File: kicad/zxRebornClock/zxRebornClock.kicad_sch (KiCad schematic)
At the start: 87 parts, among them J1 Conn_01x04, J2 Conn_01x03, J3 USB_B_Micro, Q1 MMBTA42, Q11 MMBTA42, Q2 MMBTA42, Q3 MMBTA42, Q4 MMBTA42, Q5 MMBTA42, Q6 MMBTA42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

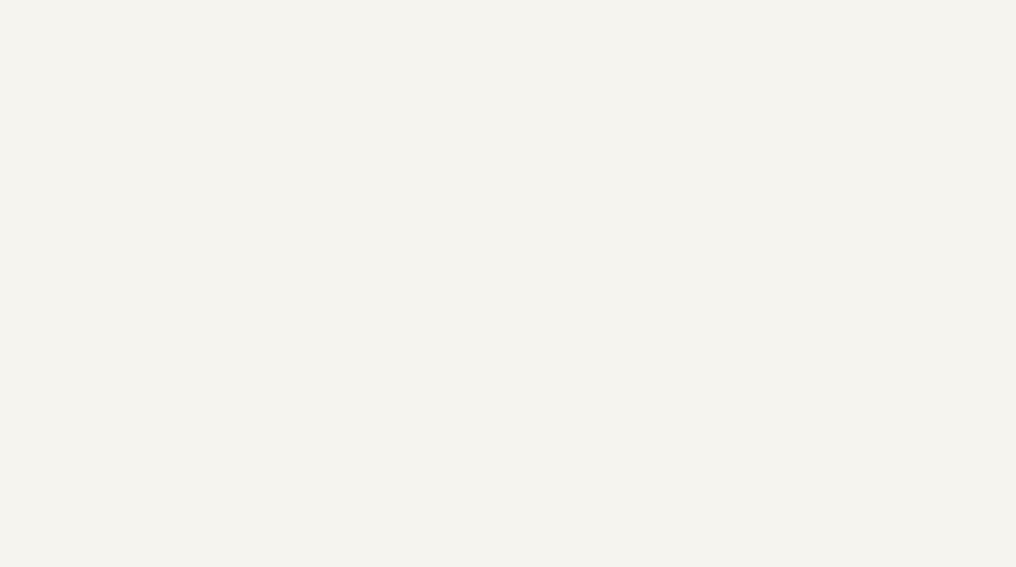
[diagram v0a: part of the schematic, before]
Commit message: add power 3.3V
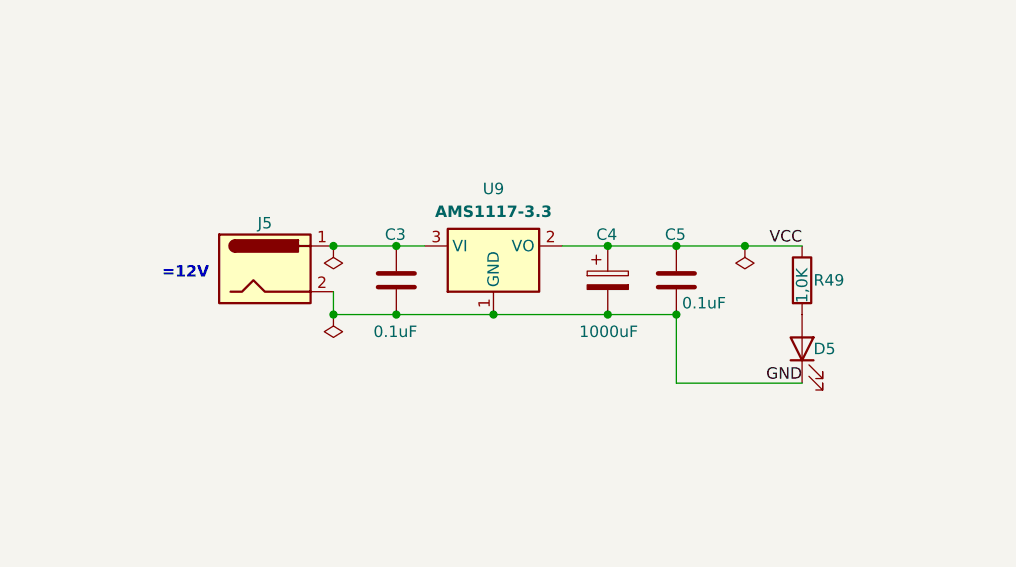
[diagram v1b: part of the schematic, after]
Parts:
- added C3, C5: 0.1uF, Capacitor_SMD:C_0805_2012Metric_Pad1.18x1.45mm_HandSolder, symbol Device:C
- added C4: 1000uF, Capacitor_THT:CP_Radial_D8.0mm_P3.50mm, symbol Device:C_Polarized
- added D5: LED, LED_SMD:LED_0805_2012Metric_Pad1.15x1.40mm_HandSolder, symbol Device:LED
- added J5: Jack DC, Connector_BarrelJack:BarrelJack_Horizontal, symbol Connector:Jack-DC
- added R49: 1,0K, Resistor_SMD:R_0805_2012Metric_Pad1.20x1.40mm_HandSolder, symbol Device:R
- added U9: AMS1117-3.3, Package_TO_SOT_SMD:SOT-223-3_TabPin2, symbol Regulator_Linear:AMS1117-5.0
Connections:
- net GND: now also C3.2, C4.2, C5.2, D5.1 (K), J5.2, U9.1 (GND)
- net VCC: now also C4.1, C5.1, R49.1, U9.2 (VO)
- new net: D5.2 (A), R49.2
- new net: C3.1, J5.1, U9.3 (VI)
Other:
- note added: "=12V"

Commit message: add some fixes
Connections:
- net VBUS: now also C3.1, J5.1, U9.3 (VI)
- net at Q7.1 (B), R26.2: now also R27.2
- net at Q1.1 (B), R2.2: now also R3.2
- net at Q8.1 (B), R28.2: now also R29.2
- net at R7.2: now also Q3.1 (B), R6.2
- net at R23.2: now also Q5.1 (B), R10.2
- net at Q2.1 (B), R4.2: now also R5.2
- net at R11.2: now also Q11.1 (B), R1.2
- net at R25.2: now also Q6.1 (B), R24.2
- net at R31.2: now also Q9.1 (B), R30.2
- net at Q4.1 (B), R8.2: now also R9.2
- no-connect marks 23 -> 37
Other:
- moved on the sheet: J5, R11, R23, R25, R27, R29, R3, R31, R5, R7, R9

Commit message: fix GPIO0 on esp12f
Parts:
- added R50: 10K, symbol Device:R
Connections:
- net VCC: now also R50.1
- net at U7.18 (GPIO0): now also R50.2
- no-connect marks 37 -> 36
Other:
- moved on the sheet: R39
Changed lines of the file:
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@@
 	)
 	(no_connect
-		(at 355.6 158.75)
-	)
-	(no_connect
 		(at 101.6 86.36)
 	)
@@
 	(wire
 		(pts
+			(xy 355.6 158.75) (xy 371.475 158.75)
+		)
+		(stroke
+			(width 0)
+			(type default)
+		)
+	)
+	(wire
+		(pts
 			(xy 355.6 36.83) (xy 355.6 27.94)
 		)
@@
 	(wire
 		(pts
+			(xy 355.6 163.83) (xy 371.475 163.83)
+		)
+		(stroke
+			(width 0)
+			(type default)
+		)
+	)
+	(wire
+		(pts
 			(xy 86.36 50.8) (xy 93.98 50.8)
 		)
@@
 		)
 	)
+	(label "VCC"
+		(at 379.095 158.75 0)
+		(effects
+			(font
+				(size 1.27 1.27)
+			)
+			(justify left bottom)
+		)
+	)
 	(label "GND"
 		(at 386.08 128.27 180)
@@
 	)
 	(label "VCC"
-		(at 363.22 163.83 0)
+		(at 379.095 163.83 0)
 		(effects
 			(font
@@
 	(symbol
 		(lib_id "Device:R")
+		(at 375.285 158.75 270)
+		(unit 1)
+		(exclude_from_sim no)
+		(in_bom yes)
+		(on_board yes)
+		(dnp no)
+		(property "Reference" "R50"
+			(at 375.031 156.718 90)
+			(effects
+				(font
+					(size 1.27 1.27)
+				)
+			)
+		)
+		(property "Value" "10K"
+			(at 375.285 158.75 90)
+			(effects
+				(font
+					(size 1.27 1.27)
+				)
+			)
+		)
+		(property "Footprint" ""
+			(at 375.285 156.972 90)
+			(effects
+				(font
+					(size 1.27 1.27)
+				)
+				(hide yes)
+			)
+		)
+		(property "Datasheet" "~"
+			(at 375.285 158.75 0)
+			(effects
+				(font
+					(size 1.27 1.27)
+				)
+				(hide yes)
+			)
+		)
+		(property "Description" "Resistor"
+			(at 375.285 158.75 0)
+			(effects
+				(font
+					(size 1.27 1.27)
+				)
+				(hide yes)
+			)
+		)
+		(pin "2"
+		)
+		(pin "1"
+		)
+		(instances
+			(project "zxRebornClock"
+				(path "/1f59fcac-59e1-4c3b-9ba4-e653e2ae108c"
+					(reference "R50")
+					(unit 1)
+				)
+			)
+		)
+	)
+	(symbol
+		(lib_id "Device:R")
 		(at 116.84 46.99 180)
 		(unit 1)
@@
 	(symbol
 		(lib_id "Device:R")
-		(at 359.41 163.83 270)
+		(at 375.285 163.83 270)
 		(unit 1)
 		(exclude_from_sim no)
@@
 		(dnp no)
 		(property "Reference" "R39"
-			(at 359.156 161.798 90)
+			(at 375.031 161.798 90)
 			(effects
 				(font
@@
 		)
 		(property "Value" "10K"
-			(at 359.41 163.83 90)
+			(at 375.285 163.83 90)
 			(effects
 				(font
@@
 		)
 		(property "Footprint" ""
-			(at 359.41 162.052 90)
+			(at 375.285 162.052 90)
 			(effects
 				(font
@@
 		)
 		(property "Datasheet" "~"
-			(at 359.41 163.83 0)
+			(at 375.285 163.83 0)
 			(effects
 				(font
@@
 		)
 		(property "Description" "Resistor"
-			(at 359.41 163.83 0)
+			(at 375.285 163.83 0)
 			(effects
 				(font

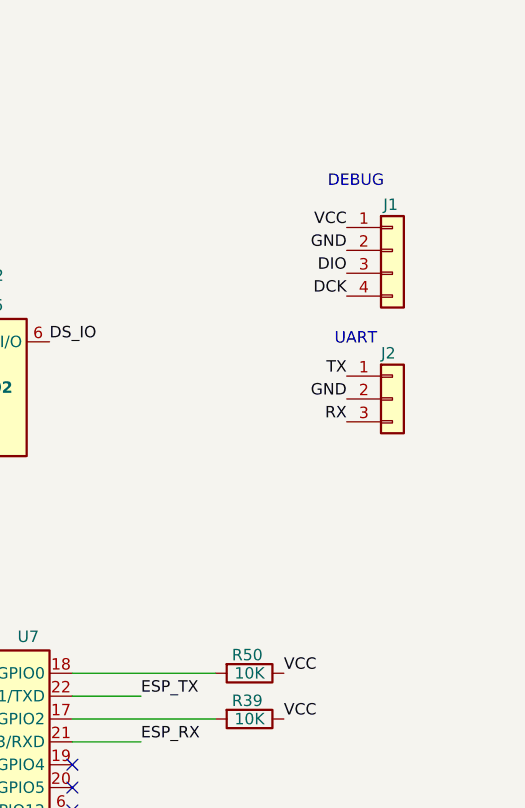
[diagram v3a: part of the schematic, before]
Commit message: add esp uart connector
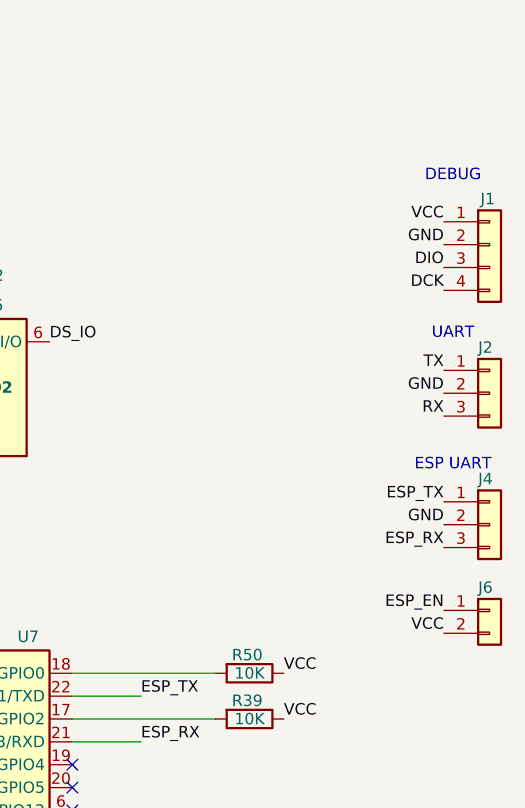
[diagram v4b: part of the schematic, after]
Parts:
- added J4: Conn_01x03, symbol Connector_Generic:Conn_01x03
- added J6: Conn_01x02, symbol Connector_Generic:Conn_01x02
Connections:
- net ESP_EN: now also J6.1 (Pin_1)
- net ESP_RX: now also J4.3 (Pin_3)
- net ESP_TX: now also J4.1 (Pin_1)
- net GND: now also J4.2 (Pin_2)
- net VCC: now also J6.2 (Pin_2)
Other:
- note added: "ESP UART"
- moved on the sheet: J1, J2
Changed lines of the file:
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@@
 	(text "DEBUG"
 		(exclude_from_sim no)
-		(at 387.096 104.14 0)
+		(at 397.891 103.505 0)
 		(effects
 			(font
@@
 	(text "UART"
 		(exclude_from_sim no)
-		(at 387.096 121.666 0)
+		(at 397.891 121.031 0)
+		(effects
+			(font
+				(size 1.27 1.27)
+			)
+		)
+	)
+	(text "ESP UART"
+		(exclude_from_sim no)
+		(at 397.891 135.636 0)
 		(effects
 			(font
@@
 	)
 	(label "DCK"
-		(at 386.08 116.84 180)
+		(at 396.875 116.205 180)
 		(effects
 			(font
@@
 		)
 	)
+	(label "VCC"
+		(at 396.875 154.305 180)
+		(effects
+			(font
+				(size 1.27 1.27)
+			)
+			(justify right bottom)
+		)
+	)
 	(label "7"
 		(at 101.6 60.96 180)
@@
 	)
 	(label "VCC"
-		(at 386.08 109.22 180)
+		(at 396.875 108.585 180)
 		(effects
 			(font
@@
 	)
 	(label "GND"
-		(at 386.08 128.27 180)
+		(at 396.875 127.635 180)
 		(effects
 			(font
@@
 	)
 	(label "RX"
-		(at 386.08 130.81 180)
+		(at 396.875 130.175 180)
 		(effects
 			(font
@@
 	)
 	(label "DIO"
-		(at 386.08 114.3 180)
+		(at 396.875 113.665 180)
 		(effects
 			(font
@@
 		)
 	)
+	(label "ESP_RX"
+		(at 396.875 144.78 180)
+		(effects
+			(font
+				(size 1.27 1.27)
+			)
+			(justify right bottom)
+		)
+	)
+	(label "ESP_EN"
+		(at 396.875 151.765 180)
+		(effects
+			(font
+				(size 1.27 1.27)
+			)
+			(justify right bottom)
+		)
+	)
 	(label "GND"
 		(at 340.36 191.77 0)
@@
 		)
 	)
+	(label "ESP_TX"
+		(at 396.875 139.7 180)
+		(effects
+			(font
+				(size 1.27 1.27)
+			)
+			(justify right bottom)
+		)
+	)
 	(label "SA3"
 		(at 246.38 106.68 90)
@@
 		)
 	)
+	(label "GND"
+		(at 396.875 142.24 180)
+		(effects
+			(font
+				(size 1.27 1.27)
+			)
+			(justify right bottom)
+		)
+	)
 	(label "8"
 		(at 110.49 69.85 0)
@@
 	)
 	(label "TX"
-		(at 386.08 125.73 180)
+		(at 396.875 125.095 180)
 		(effects
 			(font
@@
 	)
 	(label "GND"
-		(at 386.08 111.76 180)
+		(at 396.875 111.125 180)
 		(effects
 			(font
@@
 	)
 	(symbol
+		(lib_id "Connector_Generic:Conn_01x02")
+		(at 401.955 151.765 0)
+		(unit 1)
+		(exclude_from_sim no)
+		(in_bom yes)
+		(on_board yes)
+		(dnp no)
+		(property "Reference" "J6"
+			(at 400.685 149.225 0)
+			(effects
+				(font
+					(size 1.27 1.27)
+				)
+				(justify left)
+			)
+		)
+		(property "Value" "Conn_01x02"
+			(at 405.13 154.3049 0)
+			(effects
+				(font
+					(size 1.27 1.27)
+				)
+				(justify left)
+				(hide yes)
+			)
+		)
+		(property "Footprint" ""
+			(at 401.955 151.765 0)
+			(effects
+				(font
+					(size 1.27 1.27)
+				)
+				(hide yes)
+			)
+		)
+		(property "Datasheet" "~"
+			(at 401.955 151.765 0)
+			(effects
+				(font
+					(size 1.27 1.27)
+				)
+				(hide yes)
+			)
+		)
+		(property "Description" "Generic connector, single row, 01x02, script generated (kicad-library-utils/schlib/autogen/connector/)"
+			(at 401.955 151.765 0)
+			(effects
+				(font
+					(size 1.27 1.27)
+				)
+				(hide yes)
+			)
+		)
+		(pin "1"
+		)
+		(pin "2"
+		)
+		(instances
+			(project ""
+				(path "/1f59fcac-59e1-4c3b-9ba4-e653e2ae108c"
+					(reference "J6")
+					(unit 1)
+				)
+			)
+		)
+	)
+	(symbol
 		(lib_id "Device:R")
 		(at 375.285 158.75 270)
@@
 	)
 	(symbol
+		(lib_id "Connector_Generic:Conn_01x03")
+		(at 401.955 142.24 0)
+		(unit 1)
+		(exclude_from_sim no)
+		(in_bom yes)
+		(on_board yes)
+		(dnp no)
+		(property "Reference" "J4"
+			(at 400.685 137.16 0)
+			(effects
+				(font
+					(size 1.27 1.27)
+				)
+				(justify left)
+			)
+		)
+		(property "Value" "Conn_01x03"
+			(at 404.495 143.5099 0)
+			(effects
+				(font
+					(size 1.27 1.27)
+				)
+				(justify left)
+				(hide yes)
+			)
+		)
+		(property "Footprint" ""
+			(at 401.955 142.24 0)
+			(effects
+				(font
+					(size 1.27 1.27)
+				)
+				(hide yes)
+			)
+		)
+		(property "Datasheet" "~"
+			(at 401.955 142.24 0)
+			(effects
+				(font
+					(size 1.27 1.27)
+				)
+				(hide yes)
+			)
+		)
+		(property "Description" "Generic connector, single row, 01x03, script generated (kicad-library-utils/schlib/autogen/connector/)"
+			(at 401.955 142.24 0)
+			(effects
+				(font
+					(size 1.27 1.27)
+				)
+				(hide yes)
+			)
+		)
+		(pin "3"
+		)
+		(pin "2"
+		)
+		(pin "1"
+		)
+		(instances
+			(project "zxRebornClock"
+				(path "/1f59fcac-59e1-4c3b-9ba4-e653e2ae108c"
+					(reference "J4")
+					(unit 1)
+				)
+			)
+		)
+	)
+	(symbol
 		(lib_id "Device:R")
 		(at 58.42 25.4 180)
@@
 	(symbol
 		(lib_id "Connector_Generic:Conn_01x03")
-		(at 391.16 128.27 0)
+		(at 401.955 127.635 0)
 		(unit 1)
 		(exclude_from_sim no)
@@
 		(dnp no)
 		(property "Reference" "J2"
-			(at 389.89 123.19 0)
+			(at 400.685 122.555 0)
 			(effects
 				(font
@@
 		)
 		(property "Value" "Conn_01x03"
-			(at 393.7 129.5399 0)
+			(at 404.495 128.9049 0)
 			(effects
 				(font
@@
 		)
 		(property "Footprint" ""
-			(at 391.16 128.27 0)
+			(at 401.955 127.635 0)
 			(effects
 				(font
@@
 		)
 		(property "Datasheet" "~"
-			(at 391.16 128.27 0)
+			(at 401.955 127.635 0)
 			(effects
 				(font
@@
 		)
 		(property "Description" "Generic connector, single row, 01x03, script generated (kicad-library-utils/schlib/autogen/connector/)"
-			(at 391.16 128.27 0)
+			(at 401.955 127.635 0)
 			(effects
 				(font
@@
 	(symbol
 		(lib_id "Connector_Generic:Conn_01x04")
-		(at 391.16 111.76 0)
+		(at 401.955 111.125 0)
 		(unit 1)
 		(exclude_from_sim no)
@@
 		(dnp no)
 		(property "Reference" "J1"
-			(at 390.144 106.68 0)
+			(at 400.939 106.045 0)
 			(effects
 				(font
@@
 		)
 		(property "Value" "Conn_01x04"
-			(at 393.7 114.2999 0)
+			(at 404.495 113.6649 0)
 			(effects
 				(font
@@
 		)
 		(property "Footprint" ""
-			(at 391.16 111.76 0)
+			(at 401.955 111.125 0)
 			(effects
 				(font
@@
 		)
 		(property "Datasheet" "~"
-			(at 391.16 111.76 0)
+			(at 401.955 111.125 0)
 			(effects
 				(font
@@
 		)
 		(property "Description" "Generic connector, single row, 01x04, script generated (kicad-library-utils/schlib/autogen/connector/)"
-			(at 391.16 111.76 0)
+			(at 401.955 111.125 0)
 			(effects
 				(font

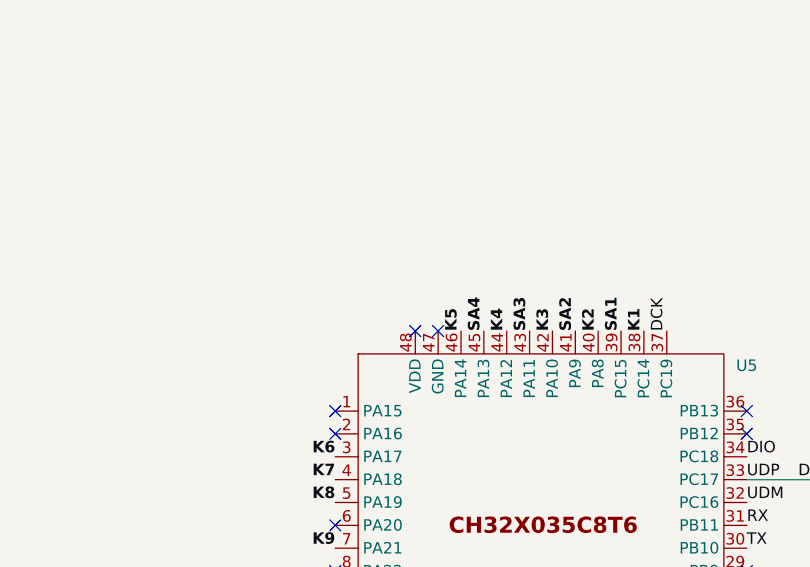
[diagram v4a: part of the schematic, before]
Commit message: add power for mcu
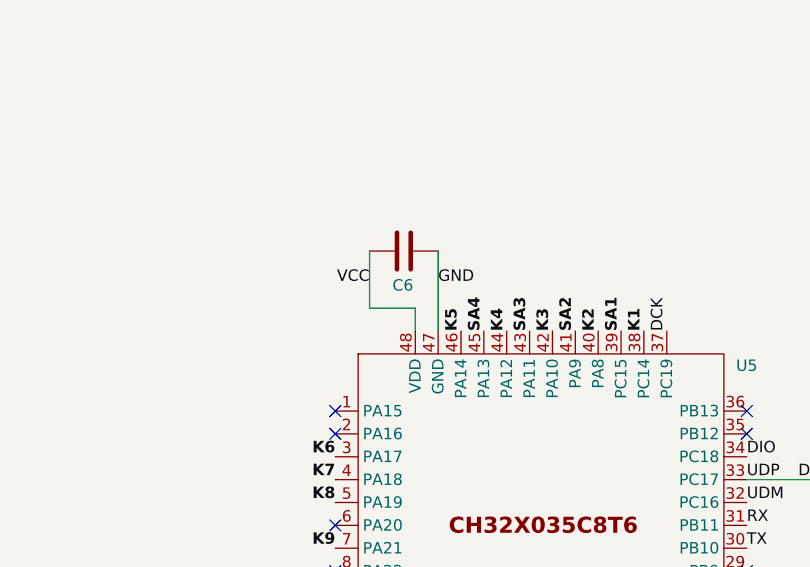
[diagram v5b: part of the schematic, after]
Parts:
- added C6: C, symbol Device:C
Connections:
- net GND: now also U5.47 (GND), C6.1
- net VCC: now also U5.48 (VDD), C6.2
- no-connect marks 36 -> 34
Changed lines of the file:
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@@
 	)
 	(no_connect
-		(at 236.22 106.68)
-	)
-	(no_connect
 		(at 270.51 118.11)
 	)
@@
 	)
 	(no_connect
-		(at 233.68 106.68)
-	)
-	(no_connect
 		(at 125.73 86.36)
 	)
@@
 	(wire
 		(pts
+			(xy 233.68 106.68) (xy 233.68 104.14)
+		)
+		(stroke
+			(width 0)
+			(type default)
+		)
+	)
+	(wire
+		(pts
 			(xy 311.15 133.35) (xy 327.66 133.35)
 		)
@@
 	(wire
 		(pts
+			(xy 228.6 97.79) (xy 228.6 104.14)
+		)
+		(stroke
+			(width 0)
+			(type default)
+		)
+	)
+	(wire
+		(pts
 			(xy 124.46 48.26) (xy 124.46 50.8)
 		)
@@
 	(wire
 		(pts
+			(xy 236.22 97.79) (xy 236.22 106.68)
+		)
+		(stroke
+			(width 0)
+			(type default)
+		)
+	)
+	(wire
+		(pts
 			(xy 55.88 50.8) (xy 63.5 50.8)
 		)
@@
 	(wire
 		(pts
+			(xy 233.68 104.14) (xy 228.6 104.14)
+		)
+		(stroke
+			(width 0)
+			(type default)
+		)
+	)
+	(wire
+		(pts
 			(xy 93.98 48.26) (xy 93.98 50.8)
 		)
@@
 		)
 	)
+	(label "GND"
+		(at 236.22 101.6 0)
+		(effects
+			(font
+				(size 1.27 1.27)
+			)
+			(justify left bottom)
+		)
+	)
 	(label "ESP_EN"
 		(at 396.875 151.765 180)
@@
 		)
 	)
+	(label "VCC"
+		(at 228.6 101.6 180)
+		(effects
+			(font
+				(size 1.27 1.27)
+			)
+			(justify right bottom)
+		)
+	)
 	(label "3"
 		(at 93.98 38.1 180)
@@
 					(unit 1)
 				)
+			)
+		)
+	)
+	(symbol
+		(lib_id "Device:C")
+		(at 232.41 97.79 270)
+		(unit 1)
+		(exclude_from_sim no)
+		(in_bom yes)
+		(on_board yes)
+		(dnp no)
+		(property "Reference" "C6"
+			(at 231.14 101.6 90)
+			(effects
+				(font
+					(size 1.27 1.27)
+				)
+				(justify left)
+			)
+		)
+		(property "Value" "C"
+			(at 231.1401 101.6 0)
+			(effects
+				(font
+					(size 1.27 1.27)
+				)
+				(justify left)
+				(hide yes)
+			)
+		)
+		(property "Footprint" ""
+			(at 228.6 98.7552 0)
+			(effects
+				(font
+					(size 1.27 1.27)
+				)
+				(hide yes)
+			)
+		)
+		(property "Datasheet" "~"
+			(at 232.41 97.79 0)
+			(effects
+				(font
+					(size 1.27 1.27)
+				)
+				(hide yes)
+			)
+		)
+		(property "Description" "Unpolarized capacitor"
+			(at 232.41 97.79 0)
+			(effects
+				(font
+					(size 1.27 1.27)
+				)
+				(hide yes)
+			)
+		)
+		(pin "1"
+		)
+		(pin "2"
+		)
+		(instances
+			(project "zxRebornClock"
+				(path "/1f59fcac-59e1-4c3b-9ba4-e653e2ae108c"
+					(reference "C6")
+					(unit 1)
+				)
